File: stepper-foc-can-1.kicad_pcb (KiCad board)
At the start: 4 copper layers, 42 x 42 mm, 84 parts, among them J1 TC2030, J2 Conn_01x02, J3 Conn_01x04_Pin, J4 Conn_01x02, J5 Conn_01x02, M1 Stepper_Motor_bipolar, SW1 SW_Push, SW2 SW_Push, SW3 SW_Push, U1 STM32G474RBTx, U2 MX25947, U3 TPS62933, U4 TCAN3413, U5 AS5047P, U6 DRV8874, U7 INA241A3IDDF, U8 DRV8874, U9 INA241A3IDDF, Y1 Crystal_GND24

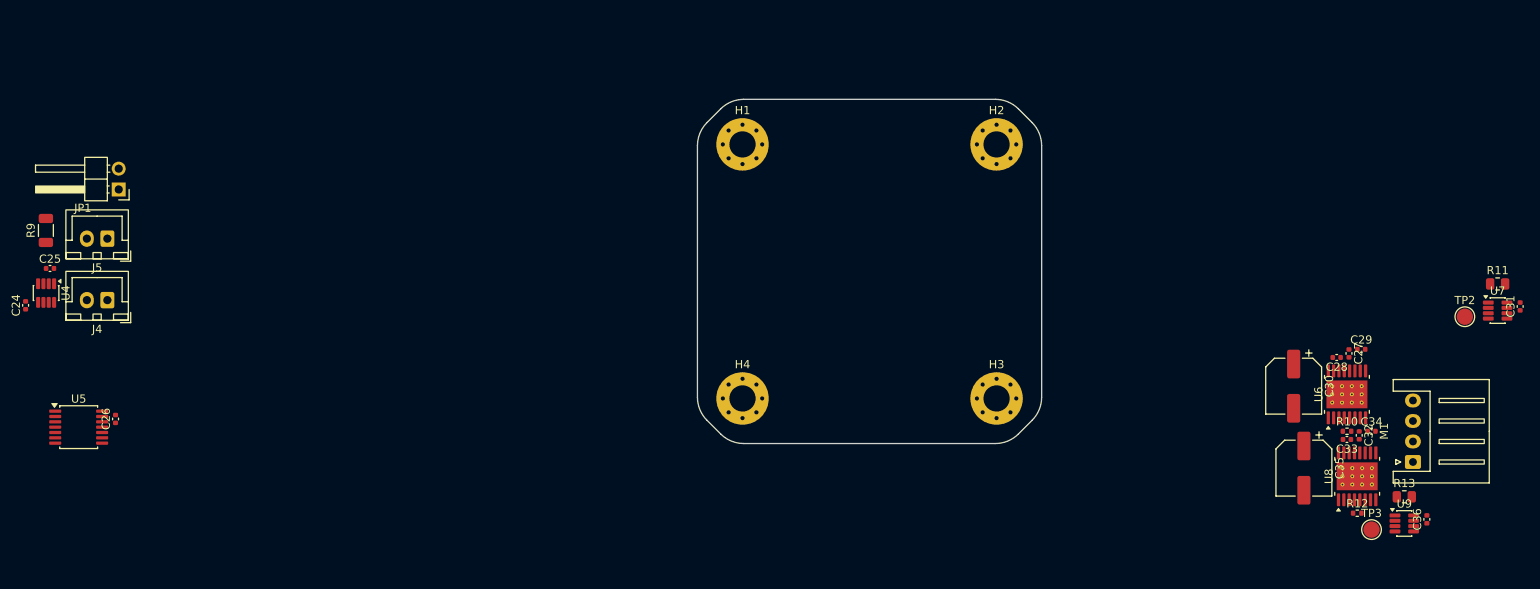
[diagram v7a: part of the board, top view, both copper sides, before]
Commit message: pcb: add drvs placement
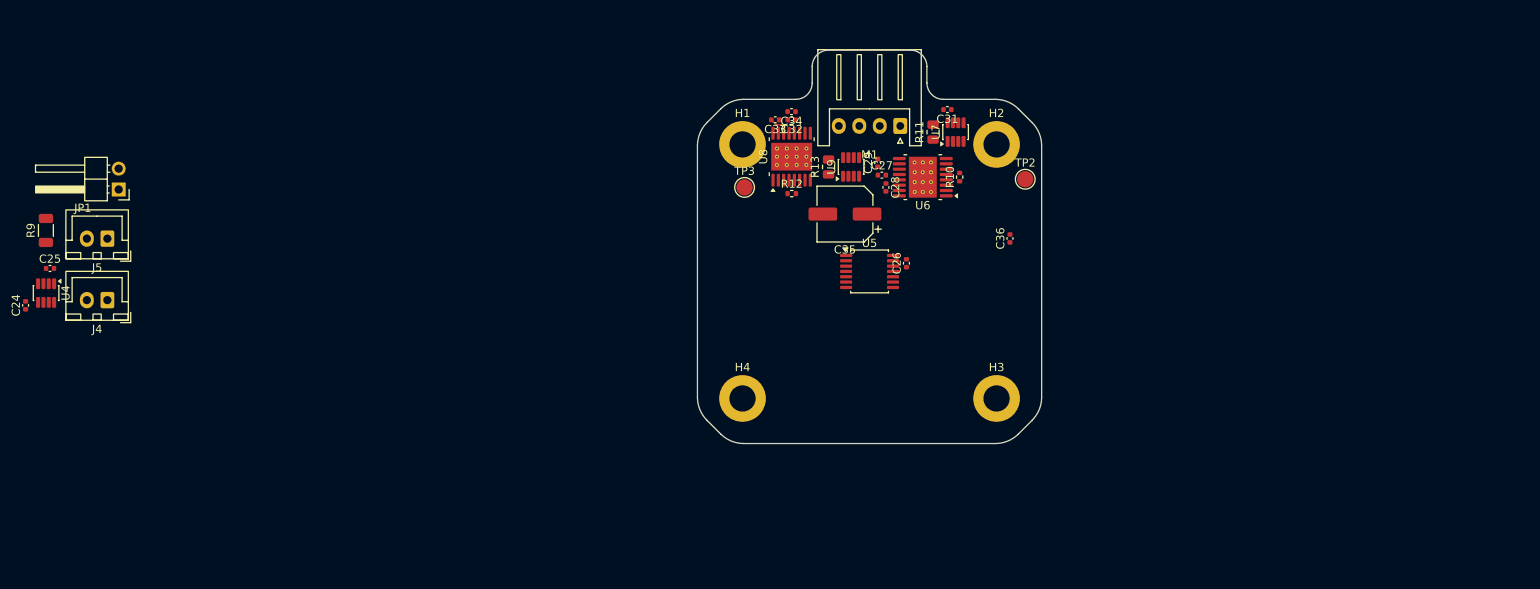
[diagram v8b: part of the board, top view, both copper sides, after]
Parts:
- removed C30: 220u, Capacitor_SMD:CP_Elec_6.3x7.7
- H1, H2, H3, H4: footprint MountingHole:MountingHole_3.2mm_M3_Pad_Via -> MountingHole:MountingHole_3.2mm_M3_ISO7380_Pad
- moved C26 98.4 mm to (148.5, 80.0)
- moved U5 98.4 mm to (144.0, 81.0)
- moved TP3 87.2 mm to (128.8, 70.8)
- moved R13 81.0 mm to (139.0, 68.2), turned to 90 degrees
- moved C34 80.8 mm to (134.5, 61.5), turned to 180 degrees
- moved U9 80.3 mm to (141.8, 68.2), turned to 90 degrees
- moved C33 79.9 mm to (132.5, 62.5)
- moved R12 79.3 mm to (134.5, 71.5)
- moved U8 79.3 mm to (134.5, 67.0)
- moved C32 79.2 mm to (134.5, 62.5), turned to 180 degrees
- moved M1 74.8 mm to (147.8, 63.2), turned to 180 degrees
- moved C31 73.9 mm to (153.5, 61.2), turned to 180 degrees
- moved R11 71.3 mm to (151.8, 64.0), turned to 90 degrees
- moved U7 69.6 mm to (154.5, 64.0), turned to 90 degrees
- moved C35 64.0 mm to (141.0, 74.0), turned to 180 degrees
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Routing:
- net Net-(U8-CPL): track 0.00 -> 2.64 mm
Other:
- board size 42 x 42 mm -> 42 x 48 mm
